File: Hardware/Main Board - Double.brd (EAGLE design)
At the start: 124.5 x 73.7 mm, 104 parts, among them J1 MICROMOD-2222-C, J10 MICRO-SD-PUSH-PUSH-EXT-PIN, J2 Vertical Qwiic Connector, J4 QWIIC_RIGHT_ANGLE, J5 CORTEX_JTAG_DEBUG_MINIMUM_PTH, J6 MICROMOD_FUNCTION_MAIN, J7 MICROMOD_FUNCTION_MAIN, Q1 3.1A/30V/105mΩ, U2 MCP73831, U5 AP7361C-33

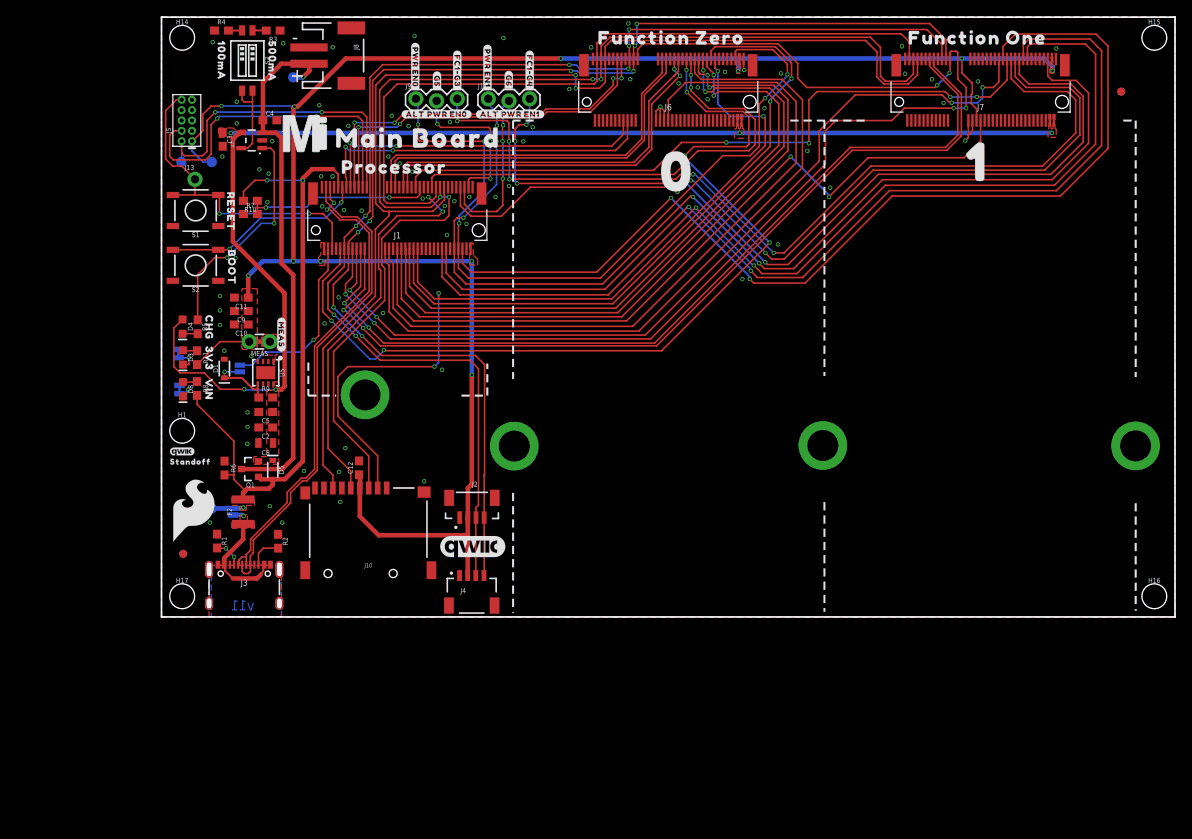
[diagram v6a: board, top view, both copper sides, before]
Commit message: Changes resistor values on LEDs, updates plexing symbol, increases capacitor value on microSD
* Adds NC jumper to shield pin on USB-C
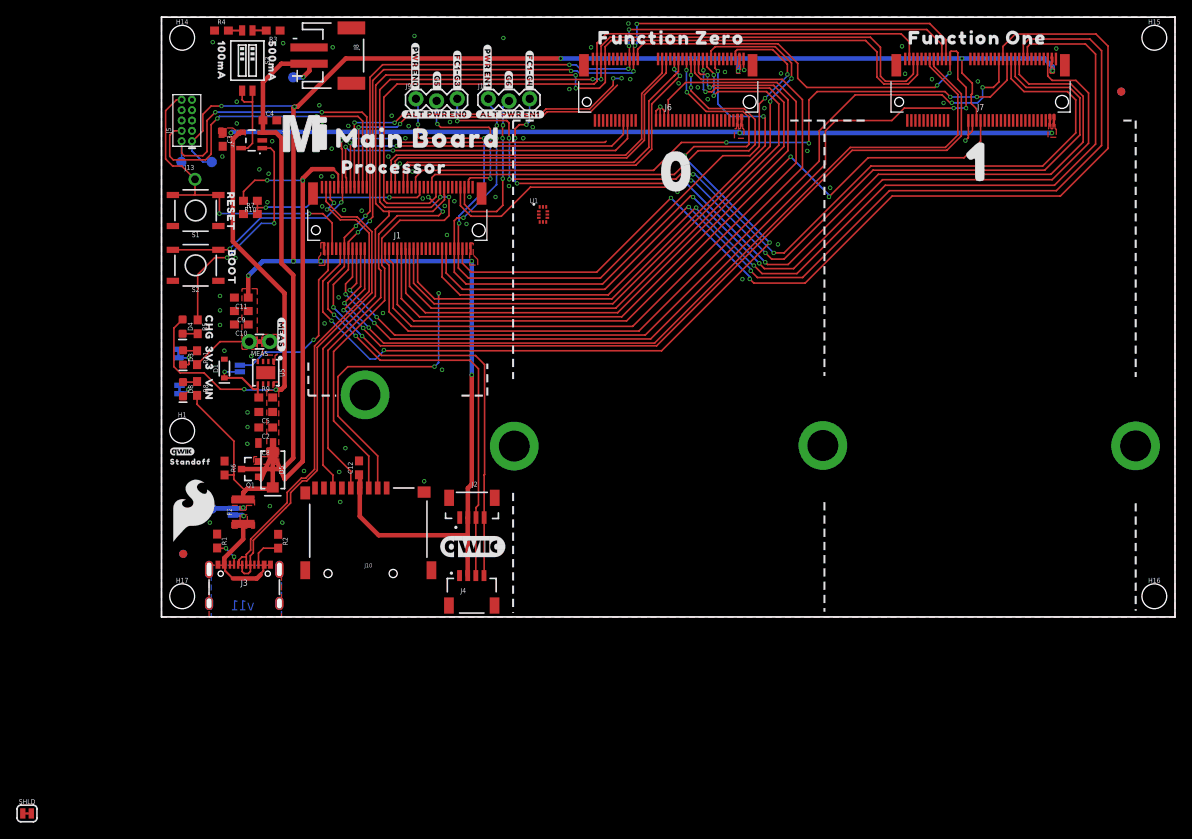
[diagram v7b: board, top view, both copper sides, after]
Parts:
- added SHLD: JUMPER-SMT_2_NC_TRACE_SILK, SparkFun-Jumpers:SMT-JUMPER_2_NC_TRACE_SILK
- added U1: STG3856QTR, dip_switch:STG3856
- C12: value 0.1uF -> 10uF
- D5: value 1A/23V/620mV -> 3A/40V/500mV; device SparkFun-DiscreteSemi:SOD-323 -> SparkFun-DiscreteSemi:SMA-DIODE
- R5: value 1k -> 4.7k
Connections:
- new net N$11: J3.SHLD1, J3.SHLD2, J3.SHLD3, J3.SHLD4, SHLD.2
- new net N$16: U1.P12
- new net N$17: U1.P10
- new net RX1-AUX_TX-PLEX-FC0: J6.6, U1.P2
- new net RX1-AUX_TX-PLEX-FC1: J7.6, U1.P3
- new net RX1-PROCESSOR-PLEX: J6.13, U1.P1
- new net TX1-AUX_RX-PLEX-FC0: J6.4, U1.P8
- new net TX1-AUX_RX-PLEX-FC1: J7.4, U1.P7
- new net TX1-PROCESSOR-PLEX: J6.15, U1.P9
- net 3.3V: now also U1.P11
- net GND: now also J6.2, J6.8, J7.2, J7.8, SHLD.1, U1.P5
- net RX1-PROCESSOR: now also U1.P4; no longer J6.13
- net TX1-PROCESSOR: now also U1.P6; no longer J6.15
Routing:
- net !BOOT!: track 25.0 -> 63.7 mm, vias 2 -> 4
- net VIN: track 81.6 -> 89.2 mm
- net RX1-PROCESSOR: track 44.6 -> 41.3 mm
- net TX1-PROCESSOR: track 45.9 -> 43.6 mm
- net GND: vias 84 -> 85

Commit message: Updates the symbol for the multiplexer and net names
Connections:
- net RX1-AUX_TX-PLEX-FC0 renamed RX1-AUX_TX-FC0-PLEX
- net RX1-AUX_TX-PLEX-FC1 renamed RX1-AUX_TX-FC1-PLEX
- net TX1-AUX_RX-PLEX-FC0 renamed TX1-AUX_RX-FC0-PLEX
- net TX1-AUX_RX-PLEX-FC1 renamed TX1-AUX_RX-FC1-PLEX
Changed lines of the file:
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@@
 <wire x1="46.333" y1="49.813" x2="55.98" y2="68.521" width="0" layer="19" extent="1-1"/>
 </signal>
-<signal name="TX1-AUX_RX-PLEX-FC0">
+<signal name="TX1-AUX_RX-FC0-PLEX">
 <contactref element="J6" pad="4"/>
 <contactref element="U1" pad="P8"/>
 <wire x1="47.383" y1="49.413" x2="53.73" y2="60.971" width="0" layer="19" extent="1-1"/>
 </signal>
-<signal name="RX1-AUX_TX-PLEX-FC1">
+<signal name="RX1-AUX_TX-FC1-PLEX">
 <contactref element="U1" pad="P3"/>
 <contactref element="J7" pad="6"/>
 <wire x1="46.333" y1="49.013" x2="92.584" y2="60.971" width="0" layer="19" extent="1-1"/>
 </signal>
-<signal name="RX1-AUX_TX-PLEX-FC0">
+<signal name="RX1-AUX_TX-FC0-PLEX">
 <contactref element="J6" pad="6"/>
 <contactref element="U1" pad="P2"/>
@@
 <wire x1="14.478" y1="1.6614" x2="14.478" y2="5.8414" width="0" layer="19" extent="1-1"/>
 </signal>
-<signal name="TX1-AUX_RX-PLEX-FC1">
+<signal name="TX1-AUX_RX-FC1-PLEX">
 <contactref element="U1" pad="P7"/>
 <contactref element="J7" pad="4"/>
